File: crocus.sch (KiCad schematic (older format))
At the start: 49 parts, among them J1 NEIGHBOR1, J2 NEIGHBOR2, J7 BONUS_ROW, P1 RP-SMA, P2 EXPANSION, T1 BALUN, U1 nRF24L01+, U2 PCA9674, Y1 XTAL

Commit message: Updated design for kicad 5.
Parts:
- C1, C2, C3, C4, C5, C6, C7: symbol C -> Device:C
- J1, J2: symbol CONN_02X20 -> Connector_Generic:Conn_02x20_Odd_Even
- J7: symbol CONN_01X20 -> Connector_Generic:Conn_01x20
- MH1, MH2, MH3, MH4: symbol CONN_01X01 -> Connector_Generic:Conn_01x01
- P1: symbol BNC -> Connector:Conn_Coaxial
- P2: symbol CONN_02X06 -> Connector_Generic:Conn_02x06_Odd_Even
- R1, R2, R3, R4, R5: symbol R -> Device:R
- T1: symbol BALUN -> gsg-symbols:BALUN
- U1: symbol nRF24L01+ -> gsg-symbols:nRF24L01+
- U2: symbol PCA9674 -> gsg-symbols:PCA9674
- W1, W10, W11, W12, W13, W14, W15, W16, W17, W18, W19, W2, W20, W21, W22, W23, W24, W3, W4, W5, W6, W7, W8, W9: symbol TEST -> Connector:TestPoint_2Pole
- Y1: symbol Crystal -> Device:Crystal
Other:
- moved on the sheet: R3, R4

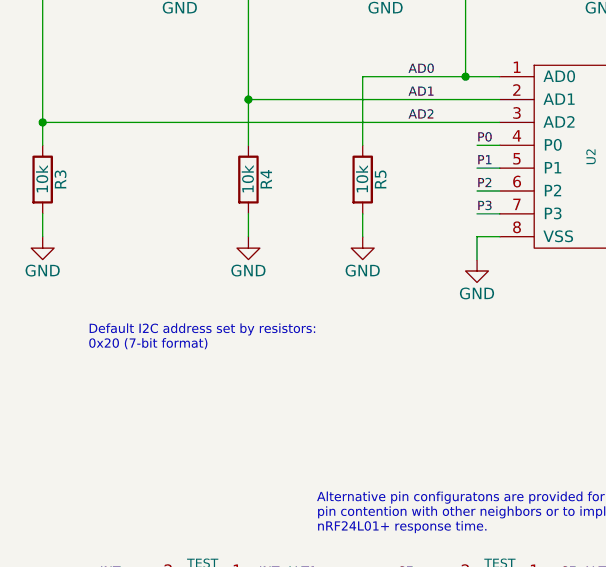
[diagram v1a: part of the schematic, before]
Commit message: Changed I2C address to 0x27
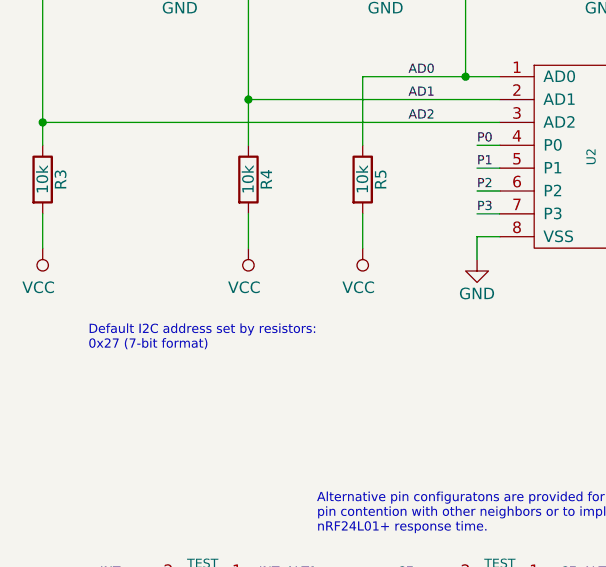
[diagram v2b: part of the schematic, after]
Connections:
- net GND: no longer R3.2, R4.2, R5.2
- net VCC: now also R3.2, R4.2, R5.2
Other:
- note added: "Default I2C address set by resistors:\n0x27 (7-bit format)"
- note removed: "Default I2C address set by resistors:\n0x20 (7-bit format)"
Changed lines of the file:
@@
 $EndComp
-Wire Wire Line
-	2000 3750 2000 3650
 Wire Wire Line
 	2000 3350 2000 3050
 Text Notes 800  4250 0    40   ~ 0
-Default I2C address set by resistors:\n0x20 (7-bit format)
+Default I2C address set by resistors:\n0x27 (7-bit format)
 Text Notes 9900 2200 0    40   ~ 0
 NMI/P4_0
@@
 $EndComp
 Connection ~ 600  3250
-Wire Wire Line
-	600  3750 600  3650
-$Comp
-L power:GND #PWR035
-U 1 1 560666F5
-P 600 3750
-F 0 "#PWR035" H 600 3500 50  0001 C CNN
-F 1 "GND" H 600 3600 50  0000 C CNN
-F 2 "" H 600 3750 60  0000 C CNN
-F 3 "" H 600 3750 60  0000 C CNN
-	1    600  3750
-	1    0    0    -1
-$EndComp
 $Comp
 L Device:R R3
@@
 	600  3250 2600 3250
 $Comp
-L power:GND #PWR036
-U 1 1 56067F1F
-P 1500 3750
-F 0 "#PWR036" H 1500 3500 50  0001 C CNN
-F 1 "GND" H 1500 3600 50  0000 C CNN
-F 2 "" H 1500 3750 60  0000 C CNN
-F 3 "" H 1500 3750 60  0000 C CNN
-	1    1500 3750
-	1    0    0    -1
-$EndComp
-$Comp
-L power:GND #PWR034
-U 1 1 56066602
-P 2000 3750
-F 0 "#PWR034" H 2000 3500 50  0001 C CNN
-F 1 "GND" H 2000 3600 50  0000 C CNN
-F 2 "" H 2000 3750 60  0000 C CNN
-F 3 "" H 2000 3750 60  0000 C CNN
-	1    2000 3750
-	1    0    0    -1
-$EndComp
-Wire Wire Line
-	1500 3750 1500 3650
-$Comp
 L Device:R R4
 U 1 1 5606618C
@@
 Wire Wire Line
 	2450 3050 2600 3050
+$Comp
+L power:VCC #PWR?
+U 1 1 5DC9DB1D
+P 600 3800
+F 0 "#PWR?" H 600 3650 50  0001 C CNN
+F 1 "VCC" H 618 3973 50  0000 C CNN
+F 2 "" H 600 3800 50  0001 C CNN
+F 3 "" H 600 3800 50  0001 C CNN
+	1    600  3800
+	-1   0    0    1
+$EndComp
+$Comp
+L power:VCC #PWR?
+U 1 1 5DC9F634
+P 1500 3800
+F 0 "#PWR?" H 1500 3650 50  0001 C CNN
+F 1 "VCC" H 1518 3973 50  0000 C CNN
+F 2 "" H 1500 3800 50  0001 C CNN
+F 3 "" H 1500 3800 50  0001 C CNN
+	1    1500 3800
+	-1   0    0    1
+$EndComp
+$Comp
+L power:VCC #PWR?
+U 1 1 5DCAC013
+P 2000 3800
+F 0 "#PWR?" H 2000 3650 50  0001 C CNN
+F 1 "VCC" H 2018 3973 50  0000 C CNN
+F 2 "" H 2000 3800 50  0001 C CNN
+F 3 "" H 2000 3800 50  0001 C CNN
+	1    2000 3800
+	-1   0    0    1
+$EndComp
+Wire Wire Line
+	600  3650 600  3800
+Wire Wire Line
+	1500 3650 1500 3800
+Wire Wire Line
+	2000 3650 2000 3800
 $EndSCHEMATC
